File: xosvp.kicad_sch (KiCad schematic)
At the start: 19 parts

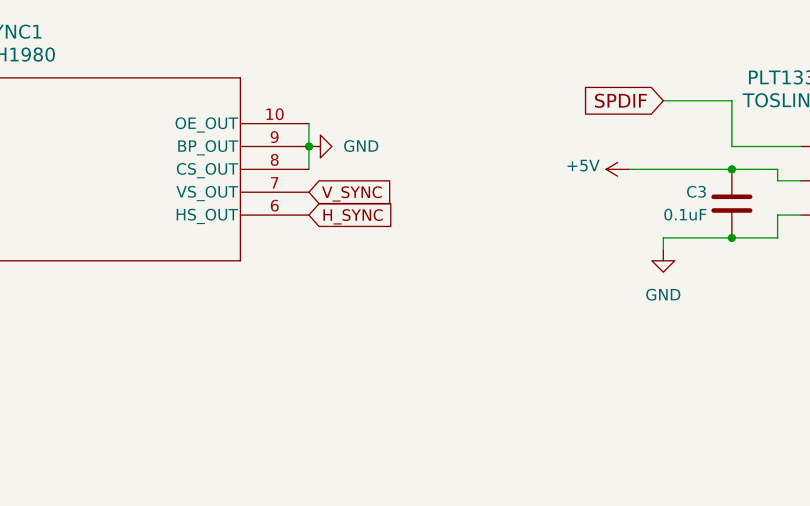
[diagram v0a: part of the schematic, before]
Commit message: Have redesigned the pcb again, realizing that the VGA connector must be flipped to prevent crossing the color signals. Have also extended the board to facilitate proper impedance matching, which was obstructed by the larger connector. Also added the 100 ohms resistors to the sync outputs as suggested by the datasheet.
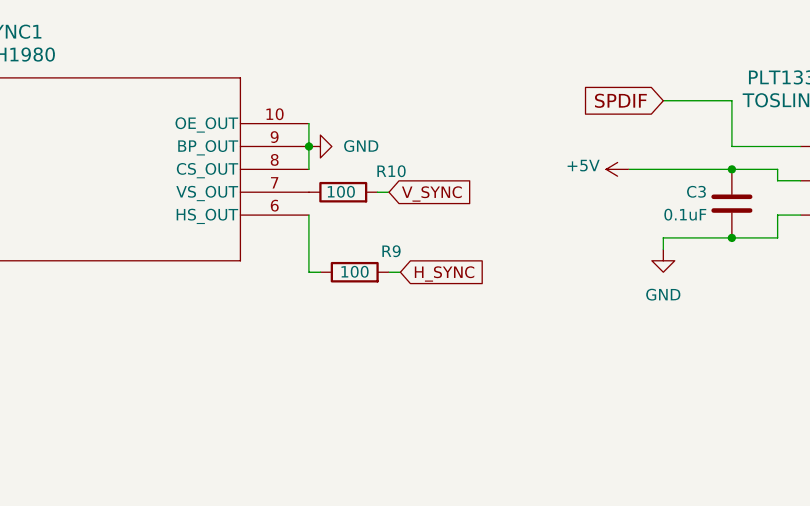
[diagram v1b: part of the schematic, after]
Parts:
- added R10, R9: 100, Resistor_SMD:R_0805_2012Metric, symbol Device:R
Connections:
- net H_SYNC: now also R9.2; no longer SYNC1.6 (HS_OUT)
- net V_SYNC: now also R10.2; no longer SYNC1.7 (VS_OUT)
- new net: R9.1, SYNC1.6 (HS_OUT)
- new net: R10.1, SYNC1.7 (VS_OUT)
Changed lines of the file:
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@@
 	(wire
 		(pts
+			(xy 210.82 35.56) (xy 209.55 35.56)
+		)
+		(stroke
+			(width 0)
+			(type default)
+		)
+	)
+	(wire
+		(pts
 			(xy 68.58 27.94) (xy 68.58 33.02)
 		)
@@
 	(wire
 		(pts
+			(xy 203.2 44.45) (xy 201.93 44.45)
+		)
+		(stroke
+			(width 0)
+			(type default)
+		)
+	)
+	(wire
+		(pts
 			(xy 106.68 38.1) (xy 109.22 38.1)
 		)
@@
 	(wire
 		(pts
+			(xy 201.93 44.45) (xy 201.93 38.1)
+		)
+		(stroke
+			(width 0)
+			(type default)
+		)
+	)
+	(wire
+		(pts
 			(xy 53.34 35.56) (xy 24.13 35.56)
 		)
@@
 	(wire
 		(pts
+			(xy 212.09 44.45) (xy 210.82 44.45)
+		)
+		(stroke
+			(width 0)
+			(type default)
+		)
+	)
+	(wire
+		(pts
 			(xy 254 38.1) (xy 256.54 38.1)
 		)
@@
 	(global_label "H_SYNC"
 		(shape input)
-		(at 201.93 38.1 0)
+		(at 212.09 44.45 0)
 		(fields_autoplaced yes)
 		(effects
@@
 		)
 		(property "Intersheetrefs" "${INTERSHEET_REFS}"
-			(at 211.4577 38.1 0)
+			(at 221.6177 44.45 0)
 			(effects
 				(font
@@
 	(global_label "V_SYNC"
 		(shape input)
-		(at 201.93 35.56 0)
+		(at 210.82 35.56 0)
 		(fields_autoplaced yes)
 		(effects
@@
 		)
 		(property "Intersheetrefs" "${INTERSHEET_REFS}"
-			(at 211.2158 35.56 0)
+			(at 220.1058 35.56 0)
 			(effects
 				(font
@@
 	)
 	(symbol
+		(lib_id "Device:R")
+		(at 207.01 44.45 90)
+		(unit 1)
+		(exclude_from_sim no)
+		(in_bom yes)
+		(on_board yes)
+		(dnp no)
+		(property "Reference" "R9"
+			(at 211.074 42.164 90)
+			(effects
+				(font
+					(size 1.27 1.27)
+				)
+			)
+		)
+		(property "Value" "100"
+			(at 207.01 44.45 90)
+			(effects
+				(font
+					(size 1.27 1.27)
+				)
+			)
+		)
+		(property "Footprint" "Resistor_SMD:R_0805_2012Metric"
+			(at 207.01 46.228 90)
+			(effects
+				(font
+					(size 1.27 1.27)
+				)
+				(hide yes)
+			)
+		)
+		(property "Datasheet" "~"
+			(at 207.01 44.45 0)
+			(effects
+				(font
+					(size 1.27 1.27)
+				)
+				(hide yes)
+			)
+		)
+		(property "Description" "Resistor"
+			(at 207.01 44.45 0)
+			(effects
+				(font
+					(size 1.27 1.27)
+				)
+				(hide yes)
+			)
+		)
+		(pin "2"
+		)
+		(pin "1"
+		)
+		(instances
+			(project ""
+				(path "/d9a19927-f308-4041-9bbb-5c98bd6ebd55"
+					(reference "R9")
+					(unit 1)
+				)
+			)
+		)
+	)
+	(symbol
 		(lib_id "power:GND")
 		(at 135.89 38.1 0)
@@
 					(unit 1)
 				)
+			)
+		)
+	)
+	(symbol
+		(lib_id "Device:R")
+		(at 205.74 35.56 90)
+		(unit 1)
+		(exclude_from_sim no)
+		(in_bom yes)
+		(on_board yes)
+		(dnp no)
+		(property "Reference" "R10"
+			(at 211.074 33.274 90)
+			(effects
+				(font
+					(size 1.27 1.27)
+				)
+			)
+		)
+		(property "Value" "100"
+			(at 205.486 35.56 90)
+			(effects
+				(font
+					(size 1.27 1.27)
+				)
+			)
+		)
+		(property "Footprint" "Resistor_SMD:R_0805_2012Metric"
+			(at 205.74 37.338 90)
+			(effects
+				(font
+					(size 1.27 1.27)
+				)
+				(hide yes)
+			)
+		)
+		(property "Datasheet" "~"
+			(at 205.74 35.56 0)
+			(effects
+				(font
+					(size 1.27 1.27)
+				)
+				(hide yes)
+			)
+		)
+		(property "Description" "Resistor"
+			(at 205.74 35.56 0)
+			(effects
+				(font
+					(size 1.27 1.27)
+				)
+				(hide yes)
+			)
+		)
+		(pin "2"
+		)
+		(pin "1"
+		)
+		(instances
+			(project "xosvp"
+				(path "/d9a19927-f308-4041-9bbb-5c98bd6ebd55"
+					(reference "R10")
+					(unit 1)
+				)
